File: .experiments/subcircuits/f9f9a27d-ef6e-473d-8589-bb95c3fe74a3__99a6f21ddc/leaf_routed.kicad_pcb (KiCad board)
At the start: 2 copper layers, 21.2 x 19.5 mm, 3 parts, among them Q1 FS8205A, U3 HY2113-KB5B, U6 LN61CN3302MR-G

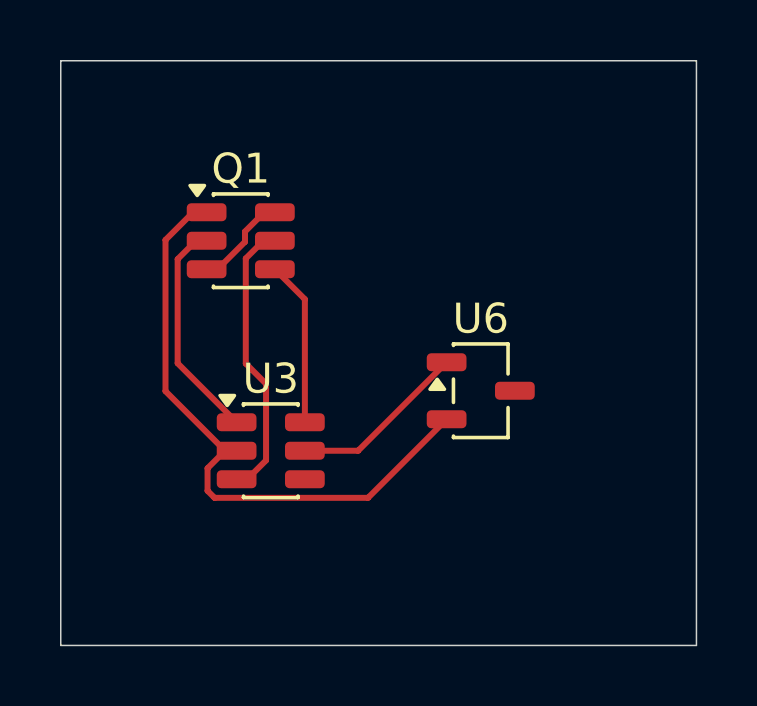
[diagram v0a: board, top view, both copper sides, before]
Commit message: feat: parent board stamping with preserved child copper
- Add --pcb, --stamp, --route, --jar flags to compose_subcircuits.py
- Implement subprocess-based parent board stamping (no pcbnew in main process)
- Add _stamp_parent_board() that copies base PCB, moves footprints to
  composed positions, clears existing tracks/zones, recreates child copper
  traces and vias with proper net name resolution
- Add _route_parent_board() for FreeRouting with preserve_existing_copper
- Add _persist_parent_artifact() for parent solved_layout.json persistence
- Store ParentComposition on ParentCompositionState for downstream access
- Update leaf artifacts from fresh pipeline run (6/6 leaves routed)
- Parent stamp verified: 37 components, 286 child traces, 10 vias preserved
  on real .kicad_pcb board with correct positions and net assignments
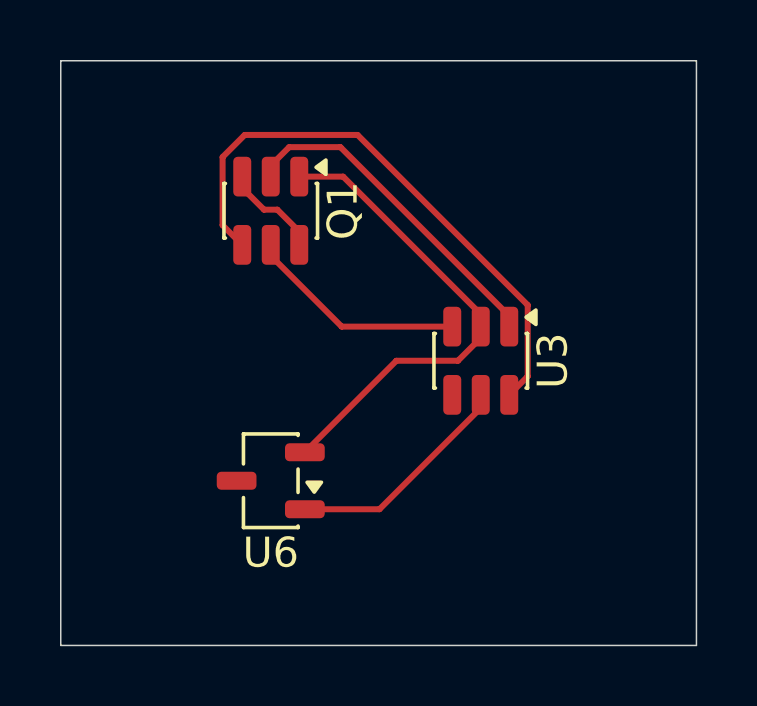
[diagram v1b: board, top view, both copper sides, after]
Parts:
- moved U3 7.62 mm to (14.0, 10.0), turned to -90 degrees
- moved U6 7.62 mm to (7.00, 14.0), turned to 180 degrees
- moved Q1 1.41 mm to (7.00, 5.00), turned to -90 degrees
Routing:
- net /CELL_NEG: track 5.51 -> 19.3 mm
- net GND: track 20.7 -> 16.2 mm
- net Net-(Q1A-G): track 7.47 -> 11.3 mm
- net Net-(Q1B-G): track 9.47 -> 7.39 mm
- net /VBAT: track 5.95 -> 7.70 mm
